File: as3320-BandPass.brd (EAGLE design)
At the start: 70.8 x 128.6 mm, 84 parts, among them IC1 CEM3320, IC2 TL074D, IC3 LM4040 5.0V, IC4 TL074D

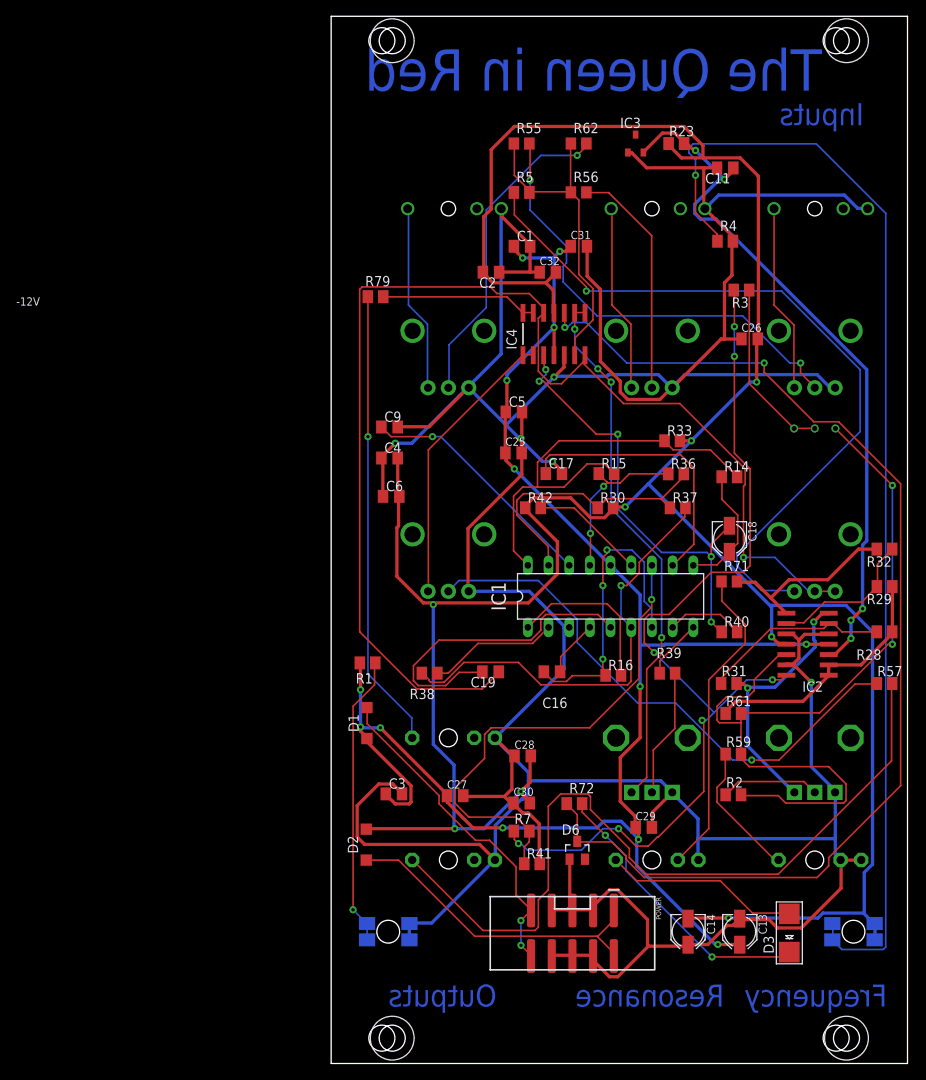
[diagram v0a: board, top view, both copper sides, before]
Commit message: Updated to include FM in
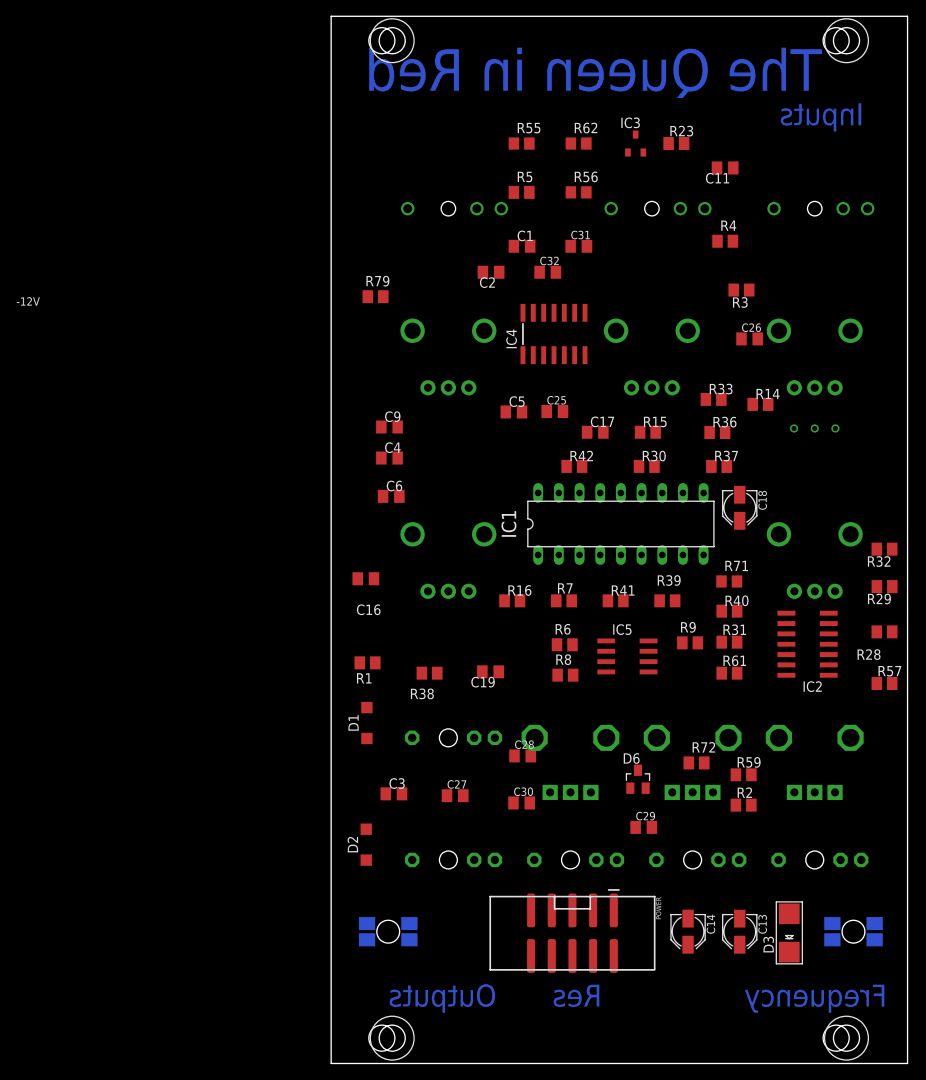
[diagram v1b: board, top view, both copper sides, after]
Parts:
- removed R55-RES2: 10kB, og-pots:ALPS_POT_VERTICAL
- added FM-LEVEL, RESONANCE: 10kB, og-pots:ALPS_POT_VERTICAL
- added FM_IN: PJ301_THONKICONN6, og-pj301_variations:WQP_PJ_301M6
- added IC5: TL072D, GMSN-R2Project:SO08
- added R6: 100k, Pure VCF:GMSN_M0805
- added R8, R9: 62k, Pure VCF:GMSN_M0805
- moved R41 33.9 mm to (-44.5, 36.8)
- moved R7 28.8 mm to (-50.8, 36.8)
- moved C16 25.6 mm to (-75.1, 39.5)
- moved R72 15.8 mm to (-34.5, 16.9)
- moved R16 15.4 mm to (-57.1, 36.8)
- moved D6 11.5 mm to (-41.7, 14.9)
- moved RES-2 10.0 mm to (-50.0, 5.00)
- moved R14 9.67 mm to (-26.7, 61.0)
- moved IC1 8.98 mm to (-43.8, 46.3)
- moved R39 8.89 mm to (-38.1, 36.8)
- moved R30 7.18 mm to (-40.6, 53.3)
- moved R37 7.18 mm to (-31.8, 53.3)
- moved R42 7.18 mm to (-49.5, 53.3)
- moved C17 7.18 mm to (-47.0, 57.5)
- moved C25 7.18 mm to (-51.9, 60.1)
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- renumbered R1-F2 to FREQUENCY
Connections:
- new net N$1: IC5.1, R6.2, R9.1
- new net N$2: IC5.2, R6.1, R8.2
- new net N$7: FM-LEVEL.P$2, IC5.3
- new net N$8: FM-LEVEL.P$1, FM_IN.P3, R8.1
- new net V+: IC5.8
- new net V-: IC5.4
- net GND: now also FM-LEVEL.P$3, FM_IN.P1, FM_IN.P2, RESONANCE.P$3; no longer R55-RES2.P$3
- net N$12: now also R9.2
- net RESONANCE_CTL2: now also RESONANCE.P$2; no longer R55-RES2.P$2
- net RESONANCE_IN2: now also RESONANCE.P$1; no longer R55-RES2.P$1
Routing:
- net GND: track 531.3 -> 0.00 mm, vias 5 -> 0
- net -12V: track 341.8 -> 0.00 mm, vias 8 -> 0
- net 12V: track 202.4 -> 0.00 mm, vias 13 -> 0
- net BANDPASS_IN: track 153.2 -> 0.00 mm, vias 1 -> 0
- net N$89: track 141.5 -> 0.00 mm, vias 2 -> 0
- net N$74: track 140.2 -> 0.00 mm, vias 1 -> 0
- net N$3: track 116.5 -> 0.00 mm, vias 7 -> 0
- net N$12: track 103.5 -> 0.00 mm, vias 2 -> 0
- net O2: track 98.4 -> 0.00 mm
- net N$20: track 92.2 -> 0.00 mm, vias 1 -> 0
- net -5VIN: track 88.0 -> 0.00 mm, vias 5 -> 0
- net N$4: track 67.9 -> 0.00 mm, vias 1 -> 0
- net RESONANCE_IN2: track 66.2 -> 0.00 mm, vias 4 -> 0
- net FREQ_IN2: track 61.2 -> 0.00 mm, vias 1 -> 0
- net N$103: track 56.5 -> 0.00 mm, vias 1 -> 0
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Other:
- board text added: "Res"
- board text removed: "Resonance"

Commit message: added power for IC5
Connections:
- removed net V+: IC5.8
- removed net V-: IC5.4
- net -12V: now also IC5.4
- net 12V: now also IC5.8
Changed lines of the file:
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@@
 <drawing>
 <settings>
-<setting alwaysvectorfont="yes"/>
+<setting alwaysvectorfont="no"/>
 <setting verticaltext="up"/>
 </settings>
@@
 <contactref element="IC1" pad="14"/>
 <contactref element="R1" pad="2"/>
-<contactref element="IC4" pad="4"/>
 <contactref element="C5" pad="1"/>
 <contactref element="C3" pad="1"/>
@@
 <contactref element="C31" pad="1"/>
 <contactref element="C29" pad="1"/>
+<contactref element="IC4" pad="4"/>
+<contactref element="IC5" pad="8"/>
 <wire x1="-75.009" y1="19.915" x2="-72.692" y2="13.118" width="0" layer="19" extent="1-1"/>
 <wire x1="-65.17" y1="12.89" x2="-72.692" y2="13.118" width="0" layer="19" extent="1-1"/>
@@
 <wire x1="-42" y1="9" x2="-65.17" y2="12.89" width="0" layer="19" extent="1-1"/>
 <wire x1="-29.21" y1="-5.41" x2="-42" y2="9" width="0" layer="19" extent="1-1"/>
-<wire x1="-52.92" y1="60.08" x2="-75.88" y2="29.21" width="0" layer="19" extent="1-1"/>
+<wire x1="-40.41" y1="31.905" x2="-42" y2="9" width="0" layer="19" extent="1-1"/>
+<wire x1="-43.81" y1="50.08" x2="-40.41" y2="31.905" width="0" layer="19" extent="1-1"/>
+<wire x1="-52.92" y1="60.08" x2="-43.81" y2="50.08" width="0" layer="19" extent="1-1"/>
 <wire x1="-57.95" y1="60.028" x2="-52.92" y2="60.08" width="0" layer="19" extent="1-1"/>
-<wire x1="-52.03" y1="67" x2="-57.95" y2="60.028" width="0" layer="19" extent="1-1"/>
+<wire x1="-52.03" y1="67" x2="-52.92" y2="60.08" width="0" layer="19" extent="1-1"/>
 <wire x1="-49.98" y1="80.38" x2="-52.03" y2="67" width="0" layer="19" extent="1-1"/>
 <wire x1="-56.95" y1="80.38" x2="-49.98" y2="80.38" width="0" layer="19" extent="1-1"/>
-<wire x1="-43.81" y1="50.08" x2="-52.92" y2="60.08" width="0" layer="19" extent="1-1"/>
-<wire x1="-18.28" y1="31.5" x2="-43.81" y2="50.08" width="0" layer="19" extent="1-1"/>
+<wire x1="-18.28" y1="31.5" x2="-40.41" y2="31.905" width="0" layer="19" extent="1-1"/>
 </signal>
 <signal name="10V" class="1">
@@
 <contactref element="LED2" pad="1"/>
 <contactref element="LED2" pad="4"/>
-<contactref element="IC4" pad="11"/>
 <contactref element="C28" pad="2"/>
 <contactref element="C26" pad="2"/>
@@
 <contactref element="C30" pad="2"/>
 <contactref element="C32" pad="2"/>
+<contactref element="IC4" pad="11"/>
+<contactref element="IC5" pad="4"/>
 <wire x1="-55" y1="12" x2="-75.09" y2="8.78" width="0" layer="19" extent="1-1"/>
 <wire x1="-54.88" y1="17.78" x2="-55" y2="12" width="0" layer="19" extent="1-1"/>
+<wire x1="-45.61" y1="28.095" x2="-54.88" y2="17.78" width="0" layer="19" extent="1-1"/>
+<wire x1="-23.48" y1="31.5" x2="-45.61" y2="28.095" width="0" layer="19" extent="1-1"/>
 <wire x1="-35.56" y1="-2.21" x2="-55" y2="12" width="0" layer="19" extent="1-1"/>
 <wire x1="-12.64" y1="-2.81" x2="-35.56" y2="-2.21" width="0" layer="19" extent="1-16"/>
 <wire x1="-12.64" y1="-4.81" x2="-12.64" y2="-2.81" width="0" layer="19" extent="16-16"/>
-<wire x1="-50.48" y1="53.34" x2="-54.88" y2="17.78" width="0" layer="19" extent="1-1"/>
+<wire x1="-50.48" y1="53.34" x2="-45.61" y2="28.095" width="0" layer="19" extent="1-1"/>
 <wire x1="-39.69" y1="53.34" x2="-50.48" y2="53.34" width="0" layer="19" extent="1-1"/>
 <wire x1="-31.47" y1="61.57" x2="-39.69" y2="53.34" width="0" layer="19" extent="1-1"/>
-<wire x1="-71.024" y1="49.663" x2="-50.48" y2="53.34" width="0" layer="19" extent="1-1"/>
-<wire x1="-71.23" y1="54.37" x2="-71.024" y2="49.663" width="0" layer="19" extent="1-1"/>
 <wire x1="-27" y1="69" x2="-31.47" y2="61.57" width="0" layer="19" extent="1-1"/>
-<wire x1="-52.03" y1="72.2" x2="-31.47" y2="61.57" width="0" layer="19" extent="1-1"/>
+<wire x1="-52.03" y1="72.2" x2="-50.48" y2="53.34" width="0" layer="19" extent="1-1"/>
 <wire x1="-51.79" y1="77.19" x2="-52.03" y2="72.2" width="0" layer="19" extent="1-1"/>
 <wire x1="-60.76" y1="77.19" x2="-51.79" y2="77.19" width="0" layer="19" extent="1-1"/>
+<wire x1="-71.23" y1="54.37" x2="-50.48" y2="53.34" width="0" layer="19" extent="1-1"/>
+<wire x1="-71.024" y1="49.663" x2="-71.23" y2="54.37" width="0" layer="19" extent="1-1"/>
 <wire x1="-37.95" y1="93" x2="-51.79" y2="77.19" width="0" layer="19" extent="1-1"/>
-<wire x1="-23.48" y1="31.5" x2="-39.69" y2="53.34" width="0" layer="19" extent="1-1"/>
 </signal>
 <signal name="-5VIN" class="1">
@@
 <wire x1="-12.38" y1="26.67" x2="-65" y2="38" width="0" layer="19" extent="1-1"/>
 </signal>
-<signal name="V+">
-<contactref element="IC5" pad="8"/>
-</signal>
-<signal name="V-">
-<contactref element="IC5" pad="4"/>
-</signal>
 <signal name="N$1">
